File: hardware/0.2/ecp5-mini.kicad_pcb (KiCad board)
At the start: 4 copper layers, 52 x 27 mm, 105 parts, among them J1 Micro_SD_Card, J2 JTAG, J3 S7 Mini, J4 S7 Mini, J5 USB_C_Receptacle_USB2.0, Q1 BSS138, Q2 BSS138, Q3 BSS138, Q4 BSS138, SW1 PTS810, U1 ECP5U_12_CABGA256, U2 TLV75525PDQNR, U3 TLV75518PDQNR, U4 USBLC6-2P6, U5 TLV62569DRLR, U6 W25Q128JVPIQ, U7 S27KS0641, U8 TLV62569DRLR, X1 DSC6101CI2A-016.0000

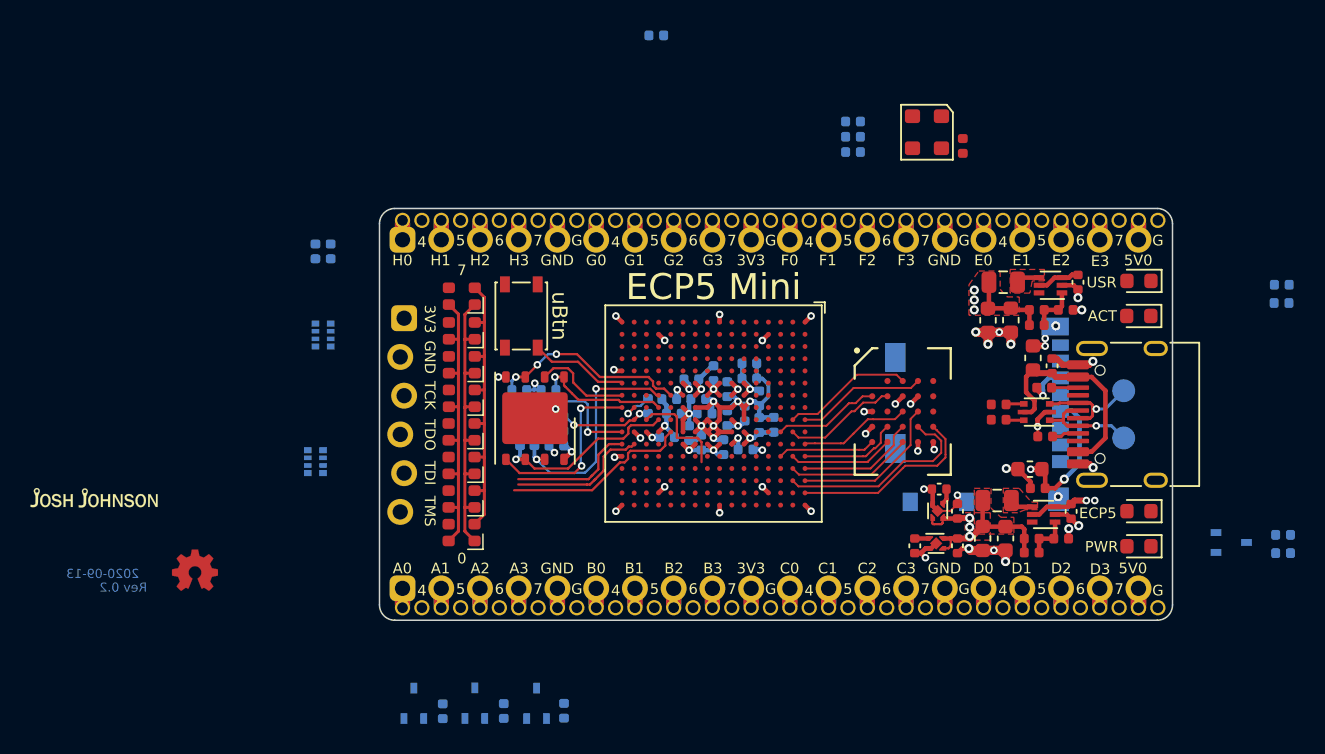
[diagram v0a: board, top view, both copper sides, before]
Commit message: half IO routed out
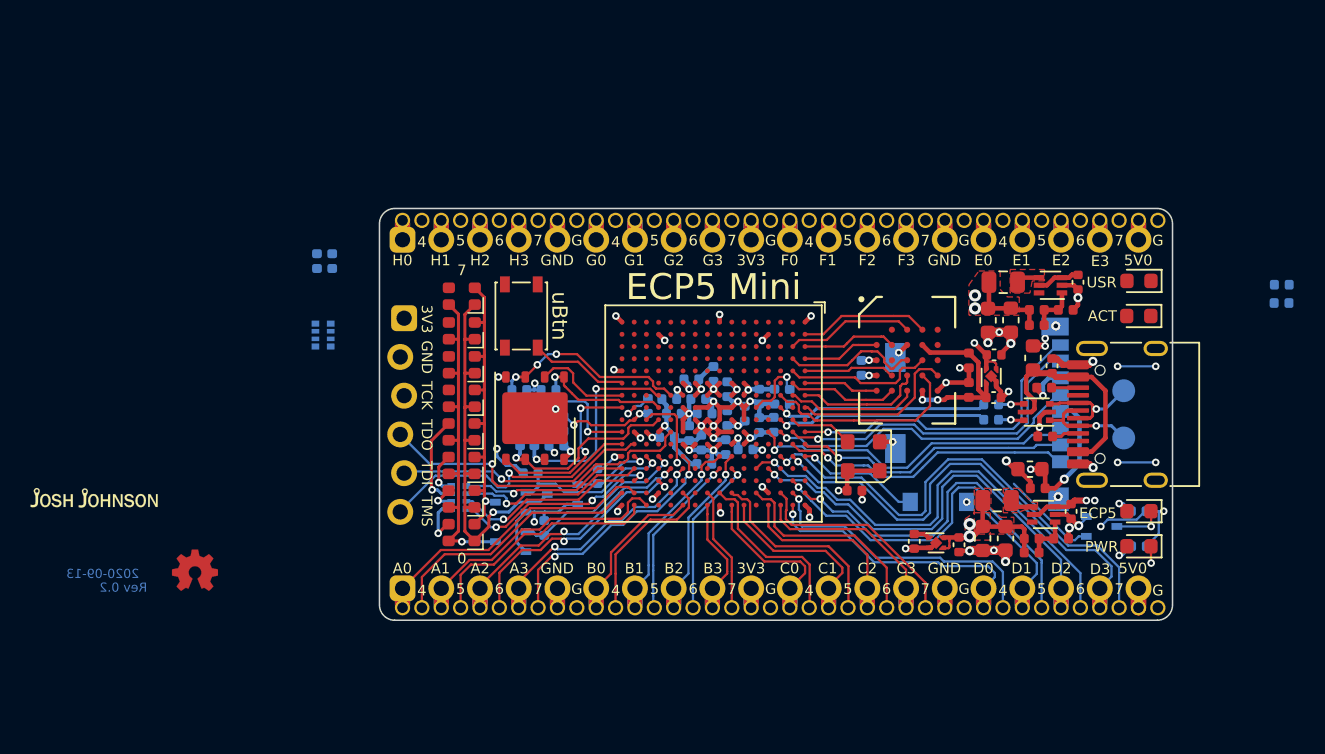
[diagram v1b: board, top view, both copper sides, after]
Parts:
- C46, C47: moved to F.Cu
- R10, R9: moved to B.Cu
- moved R11 25.3 mm to (123.1, 93.8), turned to 90 degrees
- moved C14 23.7 mm to (127.3, 100.0), turned to 0 degrees
- moved X1 21.7 mm to (128.0, 97.7), turned to 90 degrees
- moved C47 18.3 mm to (134.8, 93.3), turned to 90 degrees
- moved C46 17.4 mm to (134.8, 91.4), turned to -90 degrees
- moved R28 16.6 mm to (106.1, 98.8), turned to 180 degrees
- moved R25 15.5 mm to (110.5, 99.0)
- moved Q3 14.6 mm to (104.8, 100.7), turned to 180 degrees
- moved C45 14.2 mm to (127.8, 91.9), turned to 90 degrees
- moved Q2 13.8 mm to (108.2, 100.2), turned to 180 degrees
- moved C16 12.7 mm to (136.5, 91.0), turned to 0 degrees
- moved R30 12.3 mm to (107.0, 102.4)
- moved U3 11.5 mm to (136.3, 92.5), turned to 90 degrees
- moved C24 11.0 mm to (136.5, 93.8), turned to 0 degrees
- moved Q4 10.8 mm to (104.8, 103.3), turned to 180 degrees
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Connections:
- net /PORT_E0 renamed /PE04+
- net /PORT_E1 renamed /PE15+
- net /PORT_E2 renamed /PE26+
- net /PORT_E3 renamed /PE37+
- net /PORT_F0 renamed /PF04+
- net /PORT_F1 renamed /PF15+
- net /PORT_F2 renamed /PF26+
- net /PORT_F3 renamed /PF37+
- net /PORT_G0 renamed /PG04+
- net /PORT_G1 renamed /PG15+
- net /PORT_G2 renamed /PG26+
- net /PORT_G3 renamed /PG37+
- net /PORT_H0 renamed /PH04+
- net /PORT_H1 renamed /PH15+
- net /PORT_H2 renamed /PH26+
- net /PORT_H3 renamed /PH37+
- C19 pad 1: +3V3 -> +1V8
- C23 pad 1: +3V3 -> +1V8
- C25 pad 1: +1V8 -> +3V3
- C29 pad 1: +1V8 -> +3V3
- J1 pad 1: (no net) -> /SD_DAT2
- J1 pad 10: (no net) -> /SD_DET
- J1 pad 2: (no net) -> /SD_DAT3
- J1 pad 3: (no net) -> /SD_CMD
- J1 pad 5: (no net) -> /SD_CLK
- J1 pad 7: (no net) -> /SD_DAT0
- J1 pad 8: (no net) -> /SD_DAT1
- J3 pad 1: /PORT_A0 -> /PA04+
- J3 pad 11: /PORT_B0 -> /PB04+
- J3 pad 12: (no net) -> /PB04-
- J3 pad 13: /PORT_B1 -> /PB15+
- J3 pad 14: (no net) -> /PB15-
- J3 pad 15: /PORT_B2 -> /PB26+
- J3 pad 16: (no net) -> /PB26-
- J3 pad 17: /PORT_B3 -> /PB37+
- J3 pad 18: (no net) -> /PB37-
- J3 pad 2: (no net) -> /PA04-
- J3 pad 21: /PORT_C0 -> /PC04+
- J3 pad 22: (no net) -> /PC04-
- J3 pad 23: /PORT_C1 -> /PC15+
- J3 pad 24: (no net) -> /PC15-
- J3 pad 25: /PORT_C2 -> /PC26+
- J3 pad 26: (no net) -> /PC26-
- J3 pad 27: /PORT_C3 -> /PC37+
- J3 pad 28: (no net) -> /PC37-
- J3 pad 3: /PORT_A1 -> /PA15+
- J3 pad 31: /PORT_D0 -> /PD04+
- J3 pad 32: (no net) -> /PD04-
- J3 pad 33: /PORT_D1 -> /PD15+
- J3 pad 34: (no net) -> /PD15-
- J3 pad 35: /PORT_D2 -> /PD26+
- J3 pad 36: (no net) -> /PD26-
- J3 pad 37: /PORT_D3 -> /PD37+
- J3 pad 38: (no net) -> /PD37-
- J3 pad 4: (no net) -> /PA15-
- J3 pad 5: /PORT_A2 -> /PA26+
- J3 pad 6: (no net) -> /PA26-
- J3 pad 7: /PORT_A3 -> /PA37+
- J3 pad 8: (no net) -> /PA37-
- R11 pad 2: (no net) -> /USB_PU
- R9 pad 2: (no net) -> /USB_D-
- RN2 pad 2: Net-(D7-Pad3) -> Net-(D5-Pad3)
- RN2 pad 3: Net-(D6-Pad3) -> Net-(D7-Pad3)
- RN2 pad 4: Net-(D5-Pad3) -> Net-(D6-Pad3)
- RN2 pad 5: (no net) -> /LED_2
- RN2 pad 6: (no net) -> /LED_3
- RN2 pad 7: (no net) -> /LED_1
- RN2 pad 8: (no net) -> /LED_0
- U1 pad A10: (no net) -> /SD_DAT1
- U1 pad A11: /HR_RWDS -> /SD_DAT3
- U1 pad A12: /HR_DQ1 -> /SD_DET
- U1 pad A13: /HR_DQ0 -> (no net)
- U1 pad A14: /HR_DQ2 -> (no net)
- U1 pad A15: /HR_DQ4 -> /PD15-
- U1 pad A2: (no net) -> /HR_nRST
- U1 pad A3: (no net) -> /HR_CK
- U1 pad A4: (no net) -> /HR_nCK
- U1 pad A5: (no net) -> /HR_DQ1
- U1 pad A6: (no net) -> /HR_DQ7
- U1 pad A7: (no net) -> /HR_DQ0
- U1 pad A8: (no net) -> /HR_DQ4
- U1 pad A9: /HR_nRST -> (no net)
- U1 pad B10: /HR_CK -> /SD_DAT0
- U1 pad B11: (no net) -> /SD_DAT2
- U1 pad B12: /HR_DQ6 -> /PD37+
- U1 pad B13: /HR_DQ5 -> (no net)
- U1 pad B14: /HR_DQ3 -> /PD15+
- U1 pad B15: (no net) -> /PD04-
- U1 pad B16: (no net) -> /PD04+
- U1 pad B3: (no net) -> /HR_nCS
- U1 pad B4: (no net) -> /HR_RWDS
- U1 pad B5: (no net) -> /HR_DQ2
- U1 pad B6: (no net) -> /HR_DQ6
- U1 pad B7: (no net) -> /HR_DQ5
- U1 pad B9: /HR_nCS -> /CLK_16MHZ
- U1 pad C10: /HR_nCK -> /SD_CLK
- U1 pad C12: /HR_DQ7 -> /PD37-
- U1 pad C15: (no net) -> /PC37-
- U1 pad C16: (no net) -> /PC37+
- U1 pad C7: (no net) -> /HR_DQ3
- U1 pad C8: (no net) -> /USB_D+
- U1 pad C9: (no net) -> /USB_D-
- U1 pad D10: (no net) -> /SD_CMD
- U1 pad D13: (no net) -> /PD26+
- U1 pad D16: (no net) -> /PC26+
- U1 pad E13: (no net) -> /PD26-
- U1 pad E15: (no net) -> /PC26-
- U1 pad E8: (no net) -> /USB_PU
- U1 pad F10: +1V8 -> +3V3
- U1 pad F11: +1V8 -> +3V3
- U1 pad F16: (no net) -> /PC15+
- U1 pad F6: +3V3 -> +1V8
- U1 pad F7: +3V3 -> +1V8
- U1 pad G12: (no net) -> /PB26+
- U1 pad G13: (no net) -> /PB26-
- U1 pad G15: (no net) -> /PC15-
- U1 pad G16: (no net) -> /PC04+
- U1 pad H12: (no net) -> /PB15+
- U1 pad H13: (no net) -> /PB15-
- U1 pad H15: (no net) -> /PC04-
- U1 pad J15: (no net) -> /PB37-
- U1 pad J16: (no net) -> /PB37+
- U1 pad L12: (no net) -> /PA37-
- U1 pad L13: (no net) -> /PA37+
- U1 pad L15: (no net) -> /PB04-
- U1 pad L16: (no net) -> /PB04+
- U1 pad M13: (no net) -> /PA26+
- U1 pad N12: (no net) -> /LED_B
- U1 pad N14: (no net) -> /PA26-
- U1 pad P12: (no net) -> /LED_G
- U1 pad P16: (no net) -> /PA15+
- U1 pad R12: (no net) -> /LED_R
- U1 pad R13: (no net) -> /LED_3
- U1 pad R14: (no net) -> /LED_0
- U1 pad R15: (no net) -> /PA04+
- U1 pad R16: (no net) -> /PA15-
- U1 pad T13: (no net) -> /LED_2
- U1 pad T14: (no net) -> /LED_1
- U1 pad T15: (no net) -> /PA04-
- X1 pad 3: (no net) -> /CLK_16MHZ
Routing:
- net /PD37-: track 0.00 -> 32.4 mm, vias 0 -> 1
- net /PD26-: track 0.00 -> 30.8 mm, vias 0 -> 1
- net /PD37+: track 0.00 -> 29.8 mm, vias 0 -> 1
- net /PD26+: track 0.00 -> 27.7 mm, vias 0 -> 1
- net /PD15-: track 0.00 -> 24.9 mm, vias 0 -> 1
- net /PD15+: track 0.00 -> 24.8 mm, vias 0 -> 1
- net /SD_CMD: track 0.00 -> 21.9 mm, vias 0 -> 1
- net /SD_DAT0: track 0.00 -> 21.9 mm, vias 0 -> 1
- net /SD_DAT1: track 0.00 -> 21.1 mm, vias 0 -> 1
- net /SD_CLK: track 0.00 -> 20.8 mm, vias 0 -> 1
- net /SD_DAT2: track 0.00 -> 19.4 mm, vias 0 -> 1
- net /PD04-: track 0.00 -> 19.2 mm, vias 0 -> 1
- net GND: track 74.4 -> 93.3 mm, vias 49 -> 53
- net /SD_DAT3: track 0.00 -> 18.3 mm, vias 0 -> 1
- net /PA04+: track 0.00 -> 18.1 mm
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
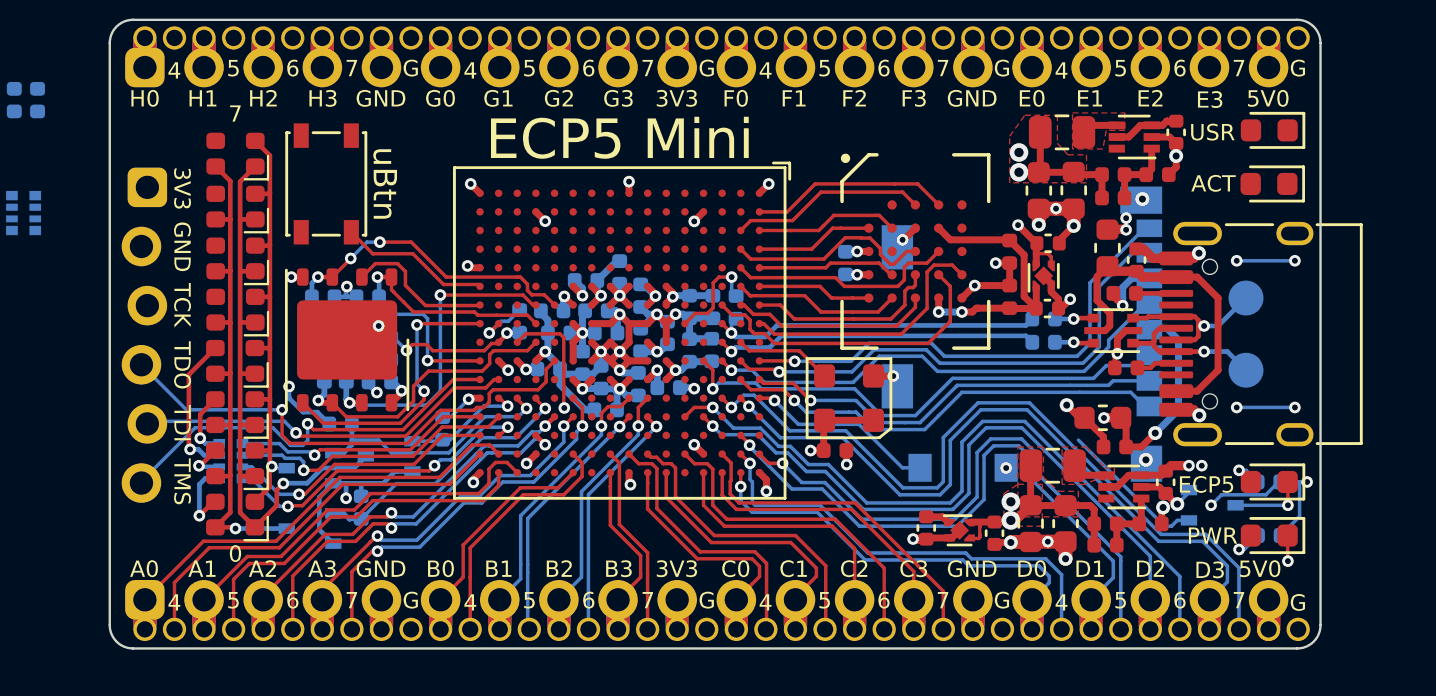
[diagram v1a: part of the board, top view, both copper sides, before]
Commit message: cleaned up diff pairs + routed power
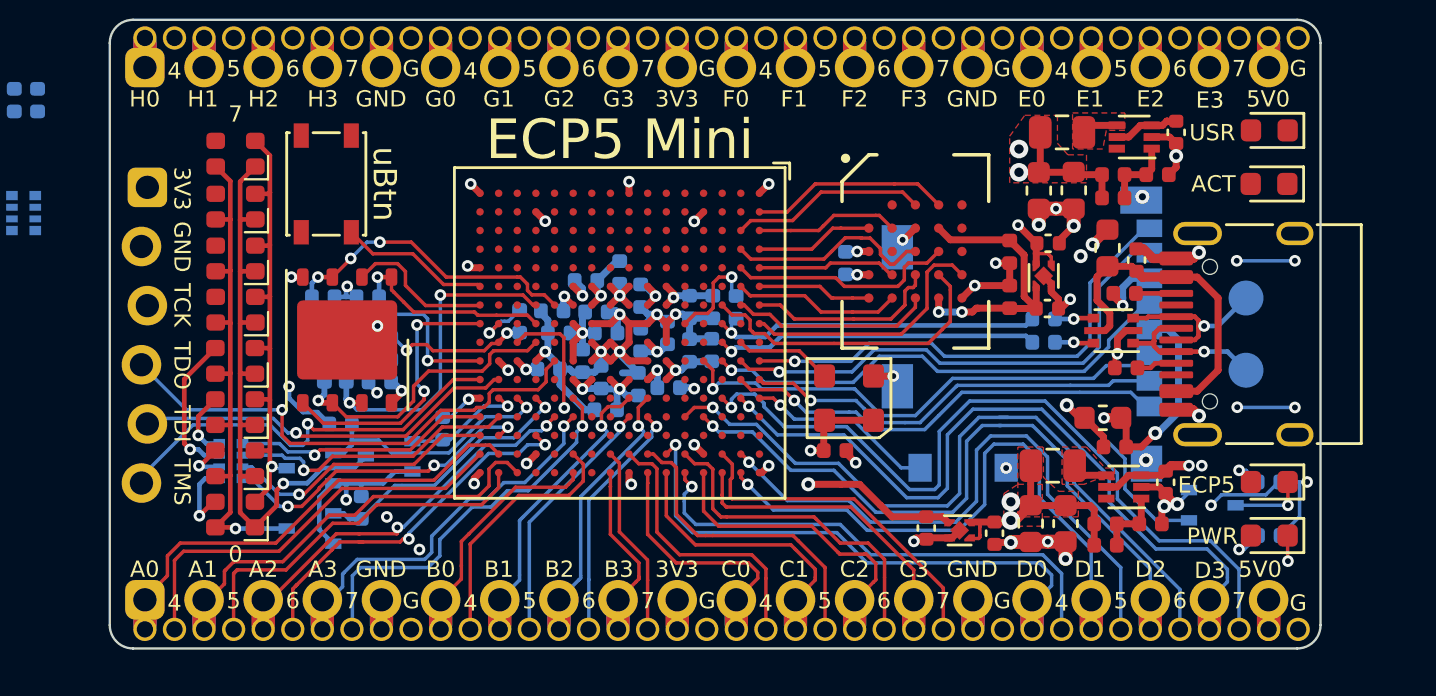
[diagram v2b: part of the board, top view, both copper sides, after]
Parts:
- moved C22 0.09 mm to (116.5, 96.1)
- moved C42 0.05 mm to (117.1, 94.0)
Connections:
- U1 pad A15: /PD15- -> (no net)
- U1 pad B14: /PD15+ -> (no net)
- U1 pad B15: /PD04- -> /PD15-
- U1 pad B16: /PD04+ -> /PD15+
- U1 pad E16: (no net) -> /PD04-
- U1 pad F15: (no net) -> /PD04+
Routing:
- net +1V1: track 14.2 -> 38.5 mm
- net +2V5: track 3.75 -> 24.7 mm, vias 2 -> 3
- net /PD04+: track 17.1 -> 22.4 mm
- net +5V: track 42.8 -> 45.4 mm
- net /PD04-: track 19.2 -> 21.7 mm
- net /PD37-: track 32.4 -> 33.8 mm
- net /PD15-: track 24.9 -> 26.2 mm
- net /PD26-: track 30.8 -> 32.0 mm
- net /PA04+: track 18.1 -> 19.3 mm
- net /PC26+: track 10.9 -> 11.9 mm
- net /PD37+: track 29.8 -> 30.7 mm
- net /PD15+: track 24.8 -> 24.0 mm
- net /FPGA Config/CFG_CDONE: track 11.7 -> 10.8 mm
- net /PD26+: track 27.7 -> 28.5 mm
- net /PA37+: track 14.8 -> 15.5 mm, vias 2 -> 1
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- added copper zone on In2.Cu, net +1V1

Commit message: routing++
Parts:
- moved C13 14.1 mm to (105.9, 87.7), turned to 180 degrees
- moved R12 13.4 mm to (105.9, 88.7), turned to 0 degrees
- moved R23 9.47 mm to (145.9, 88.5), turned to 180 degrees
- moved R22 9.38 mm to (146.0, 86.2)
- moved RN3 8.90 mm to (101.4, 89.5)
- moved C20 0.58 mm to (118.6, 96.6), turned to 0 degrees
- moved SW1 0.50 mm to (106.0, 88.5)
- moved C30 0.30 mm to (117.8, 98.2), turned to 0 degrees
- moved C38 0.10 mm to (120.3, 97.2)
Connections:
- J4 pad 12: (no net) -> /PG04-
- J4 pad 14: (no net) -> /PG15-
- J4 pad 2: (no net) -> /PH04-
- J4 pad 4: (no net) -> /PH15-
- J4 pad 6: (no net) -> /PH26-
- J4 pad 8: (no net) -> /PH37-
- RN3 pad 5: (no net) -> /LED_7
- RN3 pad 6: (no net) -> /LED_6
- RN3 pad 7: (no net) -> /LED_5
- RN3 pad 8: (no net) -> /LED_4
- U1 pad K4: (no net) -> /PG15+
- U1 pad K5: (no net) -> /PG15-
- U1 pad L1: (no net) -> /PG04+
- U1 pad L2: (no net) -> /PG04-
- U1 pad M5: (no net) -> /LED_5
- U1 pad M6: (no net) -> /LED_4
- U1 pad P1: (no net) -> /PH37+
- U1 pad P4: (no net) -> /PH15+
- U1 pad R1: (no net) -> /PH37-
- U1 pad R2: (no net) -> /PH26+
- U1 pad R3: (no net) -> /PH15-
- U1 pad R4: (no net) -> /PH04+
- U1 pad R5: (no net) -> /LED_6
- U1 pad T2: (no net) -> /PH26-
- U1 pad T3: (no net) -> /PH04-
- U1 pad T4: (no net) -> /LED_7
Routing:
- net /FPGA Config/CFG_CDONE: track 10.8 -> 38.6 mm, vias 1 -> 4
- net /PH04+: track 0.00 -> 20.5 mm
- net /PH04-: track 0.00 -> 19.3 mm
- net /PH15+: track 0.00 -> 18.8 mm, vias 0 -> 1
- net /PH15-: track 0.00 -> 18.4 mm, vias 0 -> 1
- net /LED_5: track 0.00 -> 15.4 mm, vias 0 -> 1
- net /LED_4: track 0.00 -> 15.3 mm, vias 0 -> 1
- net /PH26+: track 0.00 -> 14.1 mm
- net +1V8: track 15.6 -> 29.2 mm, vias 4 -> 5
- net /PH26-: track 0.00 -> 13.3 mm
- net /LED_6: track 0.00 -> 12.5 mm, vias 0 -> 1
- net /PH37+: track 0.00 -> 11.7 mm
- net /LED_7: track 0.00 -> 11.3 mm, vias 0 -> 1
- net /PH37-: track 0.00 -> 10.9 mm
- net /FPGA Config/TCK: track 8.95 -> 17.2 mm
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
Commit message: unrouted = 0
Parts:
- R6, R7: moved to B.Cu
- moved LOGO2 49.7 mm to (133.3, 97.9)
- moved LOGO1 40.7 mm to (118.1, 103.1)
- moved R10 9.51 mm to (126.8, 94.3)
- moved R9 9.51 mm to (126.8, 95.3)
- moved R6 6.37 mm to (145.1, 100.0), turned to 0 degrees
- moved R7 6.31 mm to (145.1, 89.8), turned to 0 degrees
- moved C20 0.22 mm to (118.5, 96.8)
- moved U4 0.10 mm to (139.3, 94.7)
- moved C9 0.09 mm to (139.0, 104.1)
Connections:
- net Net-(R10-Pad2) renamed /FPGA Config/D+
- net Net-(R9-Pad1) renamed /FPGA Config/D-
- J4 pad 16: (no net) -> /PG26-
- J4 pad 18: (no net) -> /PG37-
- J4 pad 22: (no net) -> /PF04-
- J4 pad 24: (no net) -> /PF15-
- J4 pad 26: (no net) -> /PF26-
- J4 pad 28: (no net) -> /PF37-
- J4 pad 32: (no net) -> /PE04-
- J4 pad 34: (no net) -> /PE15-
- J4 pad 36: (no net) -> /PE26-
- J4 pad 38: (no net) -> /PE37-
- R22 pad 1: (no net) -> /LED_USR
- R23 pad 1: (no net) -> /LED_ACT
- U1 pad B1: (no net) -> /LED_USR
- U1 pad B2: (no net) -> /LED_ACT
- U1 pad C1: (no net) -> /PE15+
- U1 pad C2: (no net) -> /PE15-
- U1 pad C3: (no net) -> /PE26+
- U1 pad D3: (no net) -> /PE26-
- U1 pad E1: (no net) -> /PE04-
- U1 pad E3: (no net) -> /PE37+
- U1 pad F1: (no net) -> /PF26+
- U1 pad F2: (no net) -> /PE04+
- U1 pad F3: (no net) -> /PE37-
- U1 pad G1: (no net) -> /PF15+
- U1 pad G2: (no net) -> /PF26-
- U1 pad G4: (no net) -> /PF37-
- U1 pad G5: (no net) -> /PF37+
- U1 pad H2: (no net) -> /PF15-
- U1 pad H4: (no net) -> /PG37-
- U1 pad H5: (no net) -> /PG37+
- U1 pad J1: (no net) -> /PF04+
- U1 pad J2: (no net) -> /PF04-
- U1 pad L1: /PG04+ -> /PG26+
- U1 pad L2: /PG04- -> /PG26-
- U1 pad N1: (no net) -> /PG04+
- U1 pad P2: (no net) -> /PG04-
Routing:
- net /PE37-: track 0.00 -> 31.4 mm, vias 0 -> 1
- net /PE37+: track 0.00 -> 29.5 mm, vias 0 -> 1
- net /LED_ACT: track 0.00 -> 27.7 mm, vias 0 -> 1
- net /LED_USR: track 0.00 -> 27.5 mm, vias 0 -> 1
- net /PE26-: track 0.00 -> 26.3 mm, vias 0 -> 1
- net /PE26+: track 0.00 -> 24.9 mm, vias 0 -> 1
- net /PE15-: track 0.00 -> 23.1 mm, vias 0 -> 1
- net /PF37-: track 0.00 -> 22.9 mm, vias 0 -> 1
- net /PE04-: track 0.00 -> 22.8 mm, vias 0 -> 1
- net /PE04+: track 0.00 -> 22.3 mm, vias 0 -> 1
- net /PE15+: track 0.00 -> 21.5 mm, vias 0 -> 1
- net /PF37+: track 0.00 -> 19.7 mm, vias 0 -> 1
- net /PF26-: track 0.00 -> 15.5 mm
- net /PF15-: track 0.00 -> 14.3 mm
- net /PF04-: track 0.00 -> 13.0 mm
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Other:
- board text added: "2021-01-01"
- board text removed: "2020-09-13"
